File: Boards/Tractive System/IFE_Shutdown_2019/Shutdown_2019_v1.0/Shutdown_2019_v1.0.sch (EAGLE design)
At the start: 107 parts, among them Q1 DMN6140L-7, Q11 DMP3099L-7, Q12 IRLML6346PBF, Q13 IRLML6346PBF, Q14 IRLML6346PBF, Q15 DMP3099L-7, Q16 DMN6140L-7, Q17 IRLML6346PBF, Q2 DMN6140L-7, Q3 DMN6140L-7, Q4 DMN6140L-7, Q5 DMN6140L-7, Q6 DMP3099L-7, Q7 DMN6140L-7, Q8 DMN6140L-7, Q9 DMN6140L-7, U1 STM32F103CBT6

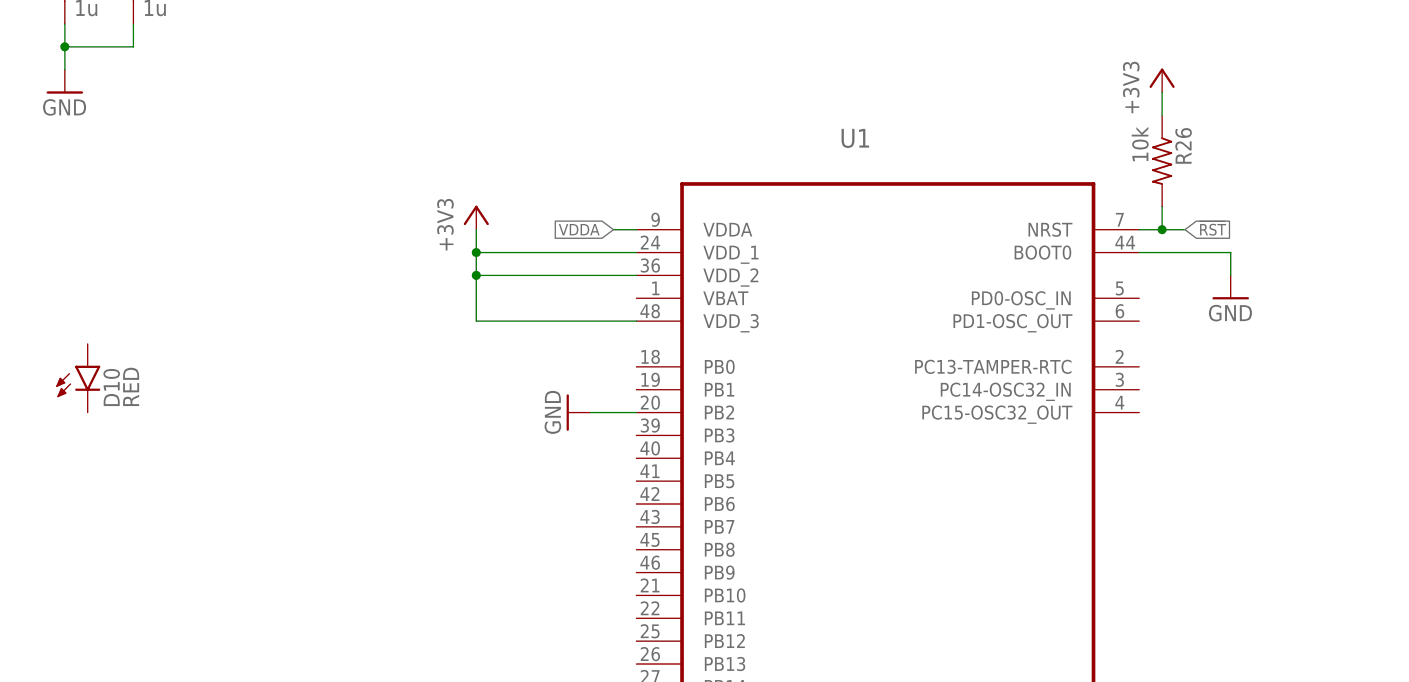
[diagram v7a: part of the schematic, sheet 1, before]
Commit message: Added digital POT for TC
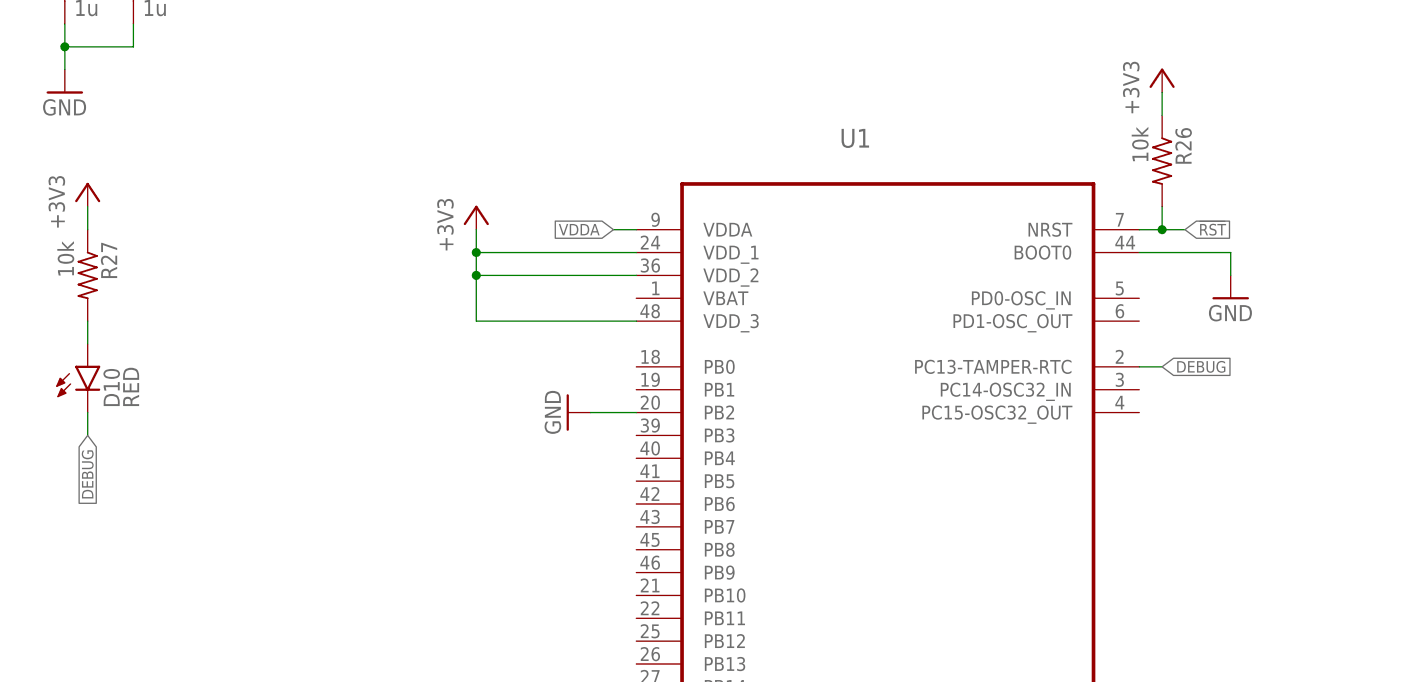
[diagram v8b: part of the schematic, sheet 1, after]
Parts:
- added R27: 10k, rcl:R-US_R0603
- added U$12: MCP4018, MICROCHIP:MCP4018
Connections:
- new net DEBUG: D10.C, U1.PC13-TAMPER-RTC
- new net N$19: D10.A, R27.2
- net +3V3: now also R27.1
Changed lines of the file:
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@@
 <part name="D11" library="SparkFun-LED" deviceset="LED-GREEN" device="0603" value="GREEN"/>
 <part name="D12" library="SparkFun-LED" deviceset="LED-GREEN" device="0603" value="GREEN"/>
+<part name="U$12" library="MICROCHIP" deviceset="MCP4018" device=""/>
+<part name="R27" library="rcl" library_urn="urn:adsk.eagle:library:334" deviceset="R-US_" device="R0603" package3d_urn="urn:adsk.eagle:package:23555/2" value="10k"/>
+<part name="+3V8" library="supply1" library_urn="urn:adsk.eagle:library:371" deviceset="+3V3" device=""/>
 </parts>
 <sheets>
@@
 <instance part="GND53" gate="1" x="167.64" y="187.96" rot="R270"/>
 <instance part="D10" gate="G$1" x="114.3" y="193.04"/>
+<instance part="R27" gate="G$1" x="114.3" y="203.2" rot="R270"/>
+<instance part="+3V8" gate="G$1" x="114.3" y="213.36"/>
 </instances>
 <busses>
@@
 <wire x1="233.68" y1="220.98" x2="233.68" y2="223.52" width="0.1524" layer="91"/>
 <pinref part="+3V9" gate="G$1" pin="+3V3"/>
+</segment>
+<segment>
+<pinref part="+3V8" gate="G$1" pin="+3V3"/>
+<pinref part="R27" gate="G$1" pin="1"/>
+<wire x1="114.3" y1="210.82" x2="114.3" y2="208.28" width="0.1524" layer="91"/>
 </segment>
 </net>
@@
 <wire x1="304.8" y1="132.08" x2="304.8" y2="129.54" width="0.1524" layer="91"/>
 <pinref part="R23" gate="G$1" pin="1"/>
+</segment>
+</net>
+<net name="DEBUG" class="0">
+<segment>
+<pinref part="U1" gate="A" pin="PC13-TAMPER-RTC"/>
+<wire x1="231.14" y1="193.04" x2="233.68" y2="193.04" width="0.1524" layer="91"/>
+<label x="233.68" y="193.04" size="1.27" layer="95" xref="yes"/>
+</segment>
+<segment>
+<pinref part="D10" gate="G$1" pin="C"/>
+<wire x1="114.3" y1="187.96" x2="114.3" y2="185.42" width="0.1524" layer="91"/>
+<label x="114.3" y="185.42" size="1.27" layer="95" rot="R270" xref="yes"/>
+</segment>
+</net>
+<net name="N$19" class="0">
+<segment>
+<pinref part="D10" gate="G$1" pin="A"/>
+<wire x1="114.3" y1="195.58" x2="114.3" y2="198.12" width="0.1524" layer="91"/>
+<pinref part="R27" gate="G$1" pin="2"/>
 </segment>
 </net>
@@
 <instance part="FRAME9" gate="G$1" x="0" y="0"/>
 <instance part="FRAME9" gate="G$2" x="325.12" y="0"/>
+<instance part="U$12" gate="G$1" x="269.24" y="162.56"/>
 </instances>
 <busses>
